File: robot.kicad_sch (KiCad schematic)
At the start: 8 parts, among them IC1 A3901SEJTR-T, J1 MOT1_OUTPUT, J2 MOT2_OUTPUT, J3 CONN_BAT, U1 MOUDLE-SEEEDUINO-XIAO-ESP32C3

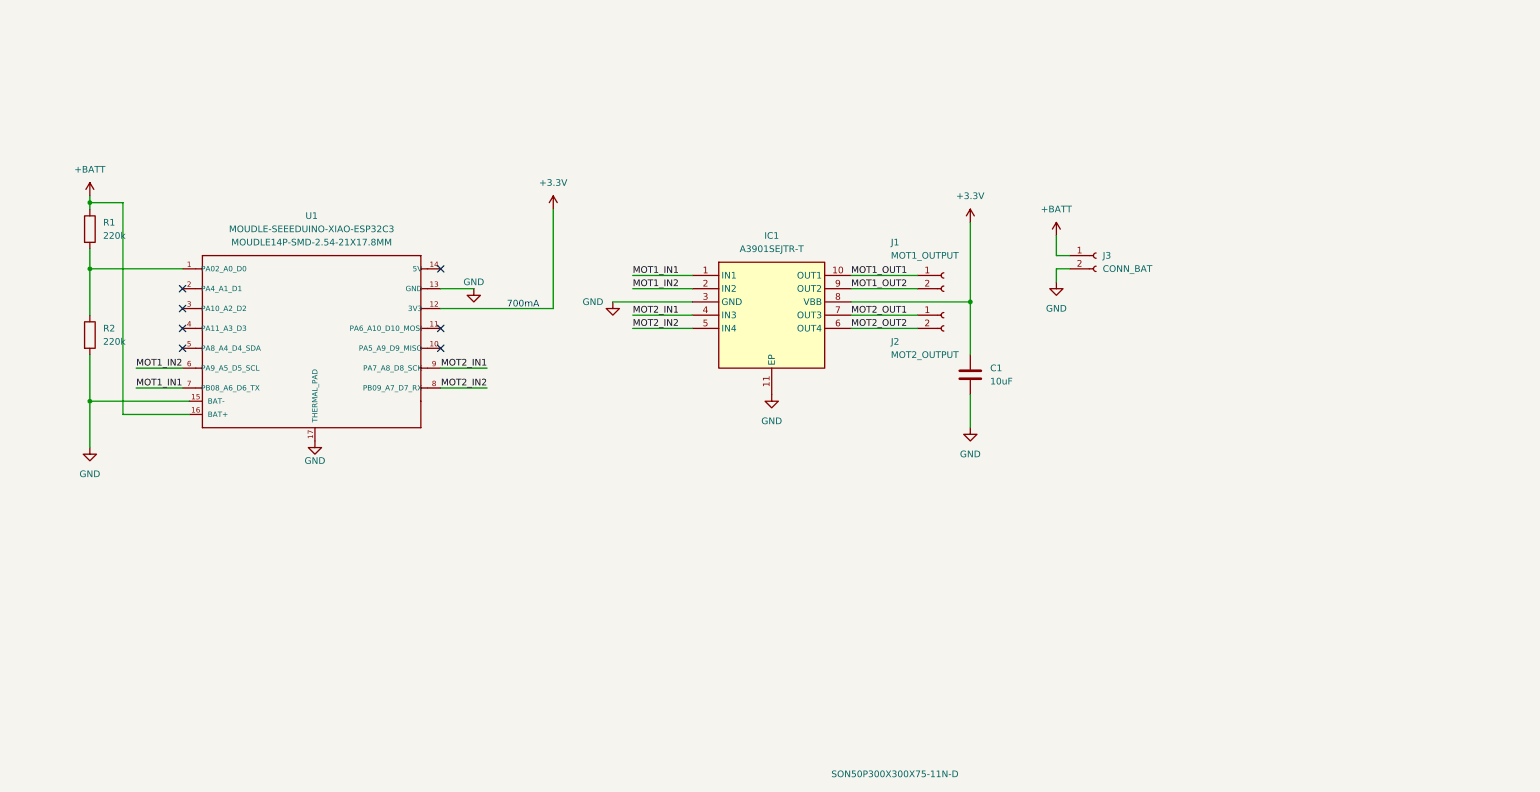
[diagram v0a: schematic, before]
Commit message: add power switch and battery voltage divider
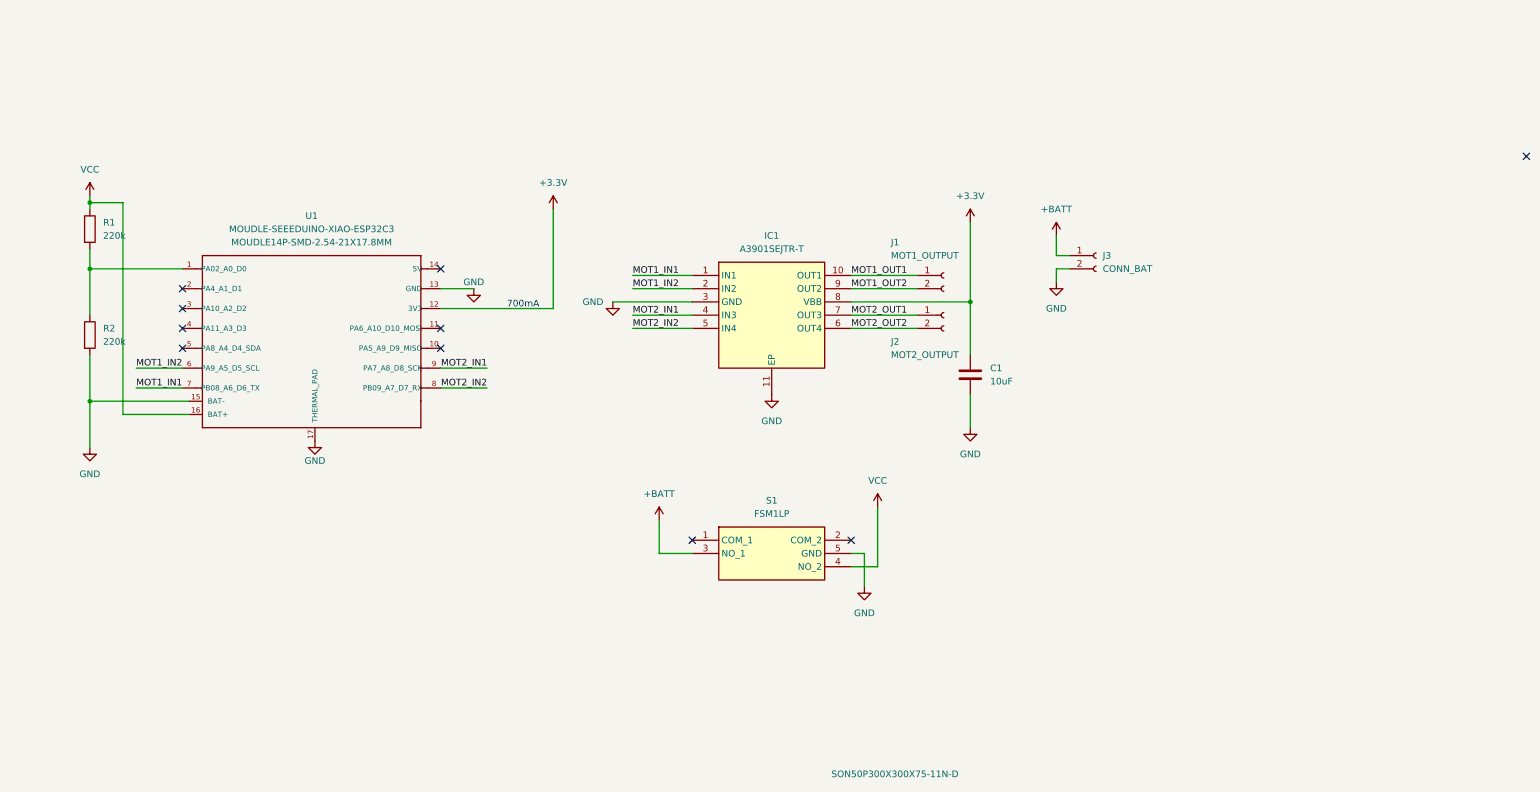
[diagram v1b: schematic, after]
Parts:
- added S1: FSM1LP, FSM1LP, symbol FSM1LP:FSM1LP
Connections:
- net +BATT: now also S1.3 (NO_1); no longer R1.1, U1.16 (BAT+)
- net GND: now also S1.5 (GND)
- new net VCC: R1.1, S1.4 (NO_2), U1.16 (BAT+)
- no-connect marks 7 -> 10
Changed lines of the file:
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@@
   (no_connect (at 74.93 80.01))
   (no_connect (at 74.93 83.82))
+  (no_connect (at 203.2 120.65))
+  (no_connect (at 332.74 46.99))
+  (no_connect (at 172.72 120.65))
   (wire (pts (xy 133.35 91.44) (xy 124.46 91.44))
     (stroke (width 0) (type default))
@@
     (stroke (width 0) (type default))
   )
+  (wire (pts (xy 203.2 125.73) (xy 208.28 125.73))
+    (stroke (width 0) (type default))
+  )
   (wire (pts (xy 203.2 69.85) (xy 215.9 69.85))
     (stroke (width 0) (type default))
@@
     (stroke (width 0) (type default))
   )
+  (wire (pts (xy 166.37 123.19) (xy 172.72 123.19))
+    (stroke (width 0) (type default))
+  )
   (wire (pts (xy 57.15 64.77) (xy 57.15 68.58))
     (stroke (width 0) (type default))
@@
     (stroke (width 0) (type default))
   )
+  (wire (pts (xy 203.2 123.19) (xy 205.74 123.19))
+    (stroke (width 0) (type default))
+  )
   (wire (pts (xy 226.06 92.71) (xy 226.06 99.06))
     (stroke (width 0) (type default))
@@
     (stroke (width 0) (type default))
   )
+  (wire (pts (xy 166.37 116.84) (xy 166.37 123.19))
+    (stroke (width 0) (type default))
+  )
   (wire (pts (xy 226.06 74.93) (xy 226.06 85.09))
     (stroke (width 0) (type default))
@@
     (stroke (width 0) (type default))
   )
+  (wire (pts (xy 208.28 125.73) (xy 208.28 114.3))
+    (stroke (width 0) (type default))
+  )
   (wire (pts (xy 66.04 91.44) (xy 74.93 91.44))
     (stroke (width 0) (type default))
@@
   )
   (wire (pts (xy 146.05 57.15) (xy 146.05 76.2))
+    (stroke (width 0) (type default))
+  )
+  (wire (pts (xy 205.74 123.19) (xy 205.74 129.54))
     (stroke (width 0) (type default))
   )
@@
         (path "/0426a851-9a02-4d3b-8136-e939d046b2a1"
           (reference "#PWR05") (unit 1)
+        )
+      )
+    )
+  )
+  (symbol (lib_id "power:VCC") (at 208.28 114.3 0) (unit 1)
+    (in_bom yes) (on_board yes) (dnp no) (fields_autoplaced)
+    (property "Reference" "#PWR012" (at 208.28 118.11 0)
+      (effects (font (size 1.27 1.27)) hide)
+    )
+    (property "Value" "VCC" (at 208.28 109.22 0)
+      (effects (font (size 1.27 1.27)))
+    )
+    (property "Footprint" "" (at 208.28 114.3 0)
+      (effects (font (size 1.27 1.27)) hide)
+    )
+    (property "Datasheet" "" (at 208.28 114.3 0)
+      (effects (font (size 1.27 1.27)) hide)
+    )
+    (pin "1")
+    (instances
+      (project "robot"
+        (path "/0426a851-9a02-4d3b-8136-e939d046b2a1"
+          (reference "#PWR012") (unit 1)
         )
       )
@@
     )
   )
+  (symbol (lib_id "power:VCC") (at 57.15 54.61 0) (unit 1)
+    (in_bom yes) (on_board yes) (dnp no) (fields_autoplaced)
+    (property "Reference" "#PWR010" (at 57.15 58.42 0)
+      (effects (font (size 1.27 1.27)) hide)
+    )
+    (property "Value" "VCC" (at 57.15 49.53 0)
+      (effects (font (size 1.27 1.27)))
+    )
+    (property "Footprint" "" (at 57.15 54.61 0)
+      (effects (font (size 1.27 1.27)) hide)
+    )
+    (property "Datasheet" "" (at 57.15 54.61 0)
+      (effects (font (size 1.27 1.27)) hide)
+    )
+    (pin "1")
+    (instances
+      (project "robot"
+        (path "/0426a851-9a02-4d3b-8136-e939d046b2a1"
+          (reference "#PWR010") (unit 1)
+        )
+      )
+    )
+  )
   (symbol (lib_id "power:GND") (at 100.33 101.6 0) (unit 1)
     (in_bom yes) (on_board yes) (dnp no)
@@
     )
   )
-  (symbol (lib_id "power:+BATT") (at 57.15 54.61 0) (unit 1)
-    (in_bom yes) (on_board yes) (dnp no) (fields_autoplaced)
-    (property "Reference" "#PWR010" (at 57.15 58.42 0)
-      (effects (font (size 1.27 1.27)) hide)
-    )
-    (property "Value" "+BATT" (at 57.15 49.53 0)
-      (effects (font (size 1.27 1.27)))
-    )
-    (property "Footprint" "" (at 57.15 54.61 0)
-      (effects (font (size 1.27 1.27)) hide)
-    )
-    (property "Datasheet" "" (at 57.15 54.61 0)
-      (effects (font (size 1.27 1.27)) hide)
-    )
-    (pin "1")
-    (instances
-      (project "robot"
-        (path "/0426a851-9a02-4d3b-8136-e939d046b2a1"
-          (reference "#PWR010") (unit 1)
-        )
-      )
-    )
-  )
   (symbol (lib_id "Device:R") (at 57.15 60.96 0) (unit 1)
     (in_bom yes) (on_board yes) (dnp no) (fields_autoplaced)
@@
         )
       )
+    )
+  )
+  (symbol (lib_id "power:+BATT") (at 166.37 116.84 0) (unit 1)
+    (in_bom yes) (on_board yes) (dnp no) (fields_autoplaced)
+    (property "Reference" "#PWR014" (at 166.37 120.65 0)
+      (effects (font (size 1.27 1.27)) hide)
+    )
+    (property "Value" "+BATT" (at 166.37 111.76 0)
+      (effects (font (size 1.27 1.27)))
+    )
+    (property "Footprint" "" (at 166.37 116.84 0)
+      (effects (font (size 1.27 1.27)) hide)
+    )
+    (property "Datasheet" "" (at 166.37 116.84 0)
+      (effects (font (size 1.27 1.27)) hide)
+    )
+    (pin "1")
+    (instances
+      (project "robot"
+        (path "/0426a851-9a02-4d3b-8136-e939d046b2a1"
+          (reference "#PWR014") (unit 1)
+        )
+      )
+    )
+  )
+  (symbol (lib_id "FSM1LP:FSM1LP") (at 172.72 120.65 0) (unit 1)
+    (in_bom yes) (on_board yes) (dnp no) (fields_autoplaced)
+    (property "Reference" "S1" (at 187.96 113.03 0)
+      (effects (font (size 1.27 1.27)))
+    )
+    (property "Value" "FSM1LP" (at 187.96 115.57 0)
+      (effects (font (size 1.27 1.27)))
+    )
+    (property "Footprint" "FSM1LP" (at 199.39 215.57 0)
+      (effects (font (size 1.27 1.27)) (justify left top) hide)
+    )
+    (property "Datasheet" "miluabraham92@gmail.com" (at 199.39 315.57 0)
+      (effects (font (size 1.27 1.27)) (justify left top) hide)
+    )
+    (property "Height" "3.4" (at 199.39 515.57 0)
+      (effects (font (size 1.27 1.27)) (justify left top) hide)
+    )
+    (property "Manufacturer_Name" "TE Connectivity" (at 199.39 615.57 0)
+      (effects (font (size 1.27 1.27)) (justify left top) hide)
+    )
+    (property "Manufacturer_Part_Number" "FSM1LP" (at 199.39 715.57 0)
+      (effects (font (size 1.27 1.27)) (justify left top) hide)
+    )
+    (property "Mouser Part Number" "506-FSM1LP" (at 199.39 815.57 0)
+      (effects (font (size 1.27 1.27)) (justify left top) hide)
+    )
+    (property "Mouser Price/Stock" "https://www.mouser.co.uk/ProductDetail/TE-Connectivity-PB/FSM1LP?qs=X41HXGMJECpfKcLAbtysig%3D%3D" (at 199.39 915.57 0)
+      (effects (font (size 1.27 1.27)) (justify left top) hide)
+    )
+    (property "Arrow Part Number" "FSM1LP" (at 199.39 1015.57 0)
+      (effects (font (size 1.27 1.27)) (justify left top) hide)
+    )
+    (property "Arrow Price/Stock" "https://www.arrow.com/en/products/fsm1lp/te-connectivity?region=nac" (at 199.39 1115.57 0)
+      (effects (font (size 1.27 1.27)) (justify left top) hide)
+    )
+    (pin "2")
+    (pin "1")
+    (pin "5")
+    (pin "4")
+    (pin "3")
+    (instances
+      (project "robot"
+        (path "/0426a851-9a02-4d3b-8136-e939d046b2a1"
+          (reference "S1") (unit 1)
+        )
+      )
+    )
+  )
+  (symbol (lib_id "power:GND") (at 205.74 129.54 0) (unit 1)
+    (in_bom yes) (on_board yes) (dnp no) (fields_autoplaced)
+    (property "Reference" "#PWR013" (at 205.74 135.89 0)
+      (effects (font (size 1.27 1.27)) hide)
+    )
+    (property "Value" "GND" (at 205.74 134.62 0)
+      (effects (font (size 1.27 1.27)))
+    )
+    (property "Footprint" "" (at 205.74 129.54 0)
+      (effects (font (size 1.27 1.27)) hide)
+    )
+    (property "Datasheet" "" (at 205.74 129.54 0)
+      (effects (font (size 1.27 1.27)) hide)
+    )
+    (pin "1")
+    (instances
+      (project "robot"
+        (path "/0426a851-9a02-4d3b-8136-e939d046b2a1"
+          (reference "#PWR013") (unit 1)
+        )
+      )

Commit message: 6-switch dipswitch for misc. configuration
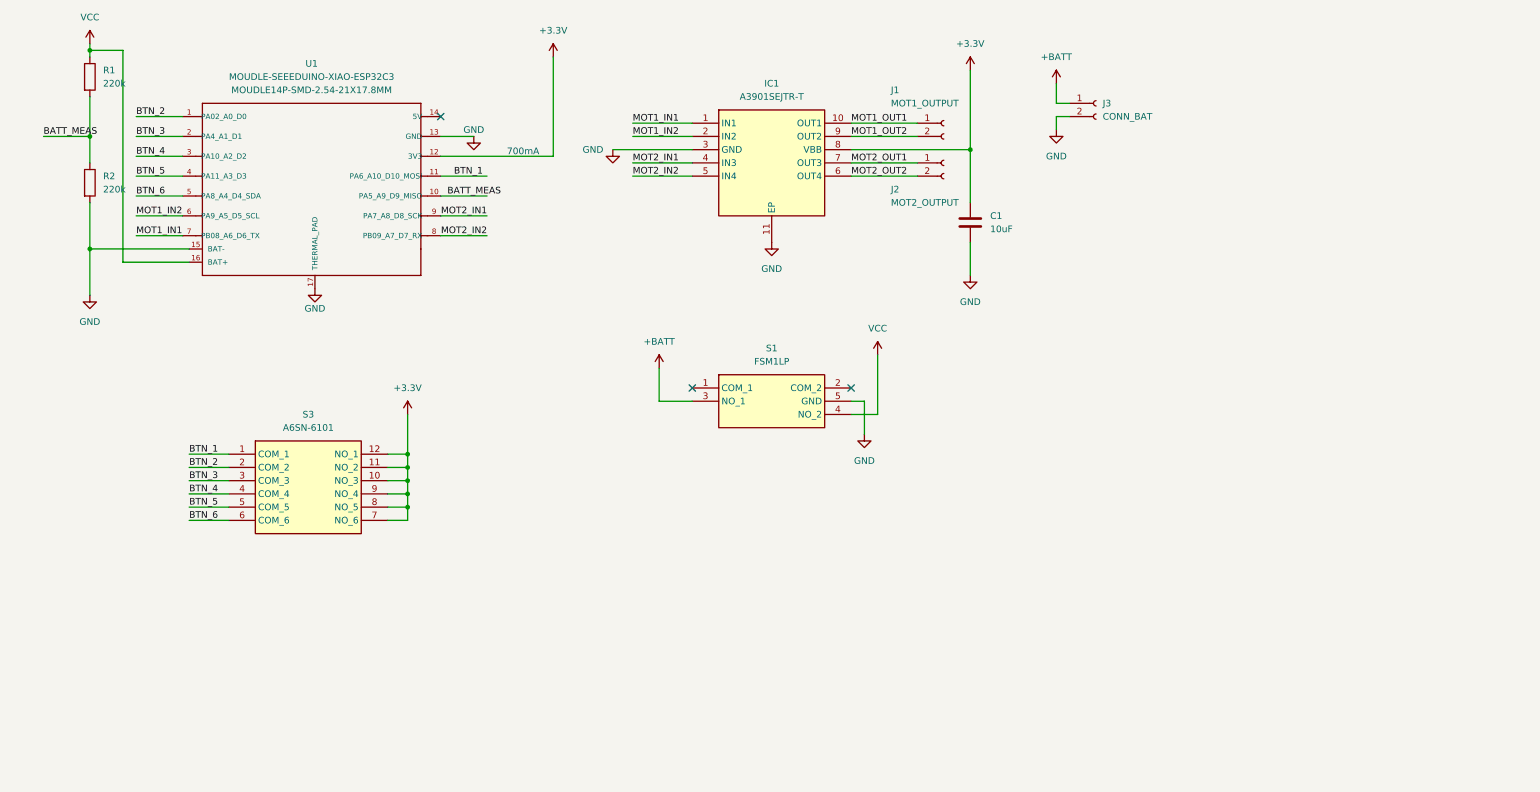
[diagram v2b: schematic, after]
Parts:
- added S3: A6SN-6101, A6SN6101, symbol A6SN-6101:A6SN-6101
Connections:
- net +3.3V: now also S3.10 (NO_3), S3.11 (NO_2), S3.12 (NO_1), S3.7 (NO_6), S3.8 (NO_5), S3.9 (NO_4)
- net BATT_MEAS: now reaches R1.2, R2.1
- net BATT_MEAS: now also U1.10 (PA5_A9_D9_MISO); no longer U1.1 (PA02_A0_D0)
- net BTN_1: now reaches U1.11 (PA6_A10_D10_MOSI)
- net BTN_1: now also S3.1 (COM_1)
- net BTN_3: now reaches U1.2 (PA4_A1_D1)
- net BTN_3: now also S3.3 (COM_3)
- net BTN_4: now reaches U1.3 (PA10_A2_D2)
- net BTN_4: now also S3.4 (COM_4)
- net BTN_5: now reaches U1.4 (PA11_A3_D3)
- net BTN_5: now also S3.5 (COM_5)
- net BTN_6: now reaches U1.5 (PA8_A4_D4_SDA)
- net BTN_6: now also S3.6 (COM_6)
- new net BTN_2: S3.2 (COM_2), U1.1 (PA02_A0_D0)
- no-connect marks 10 -> 3
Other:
- moved on the sheet: C1, IC1, J1, J2, J3, R1, R2, S1, U1

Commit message: 4-switch dipswitch, LEDs, reorder
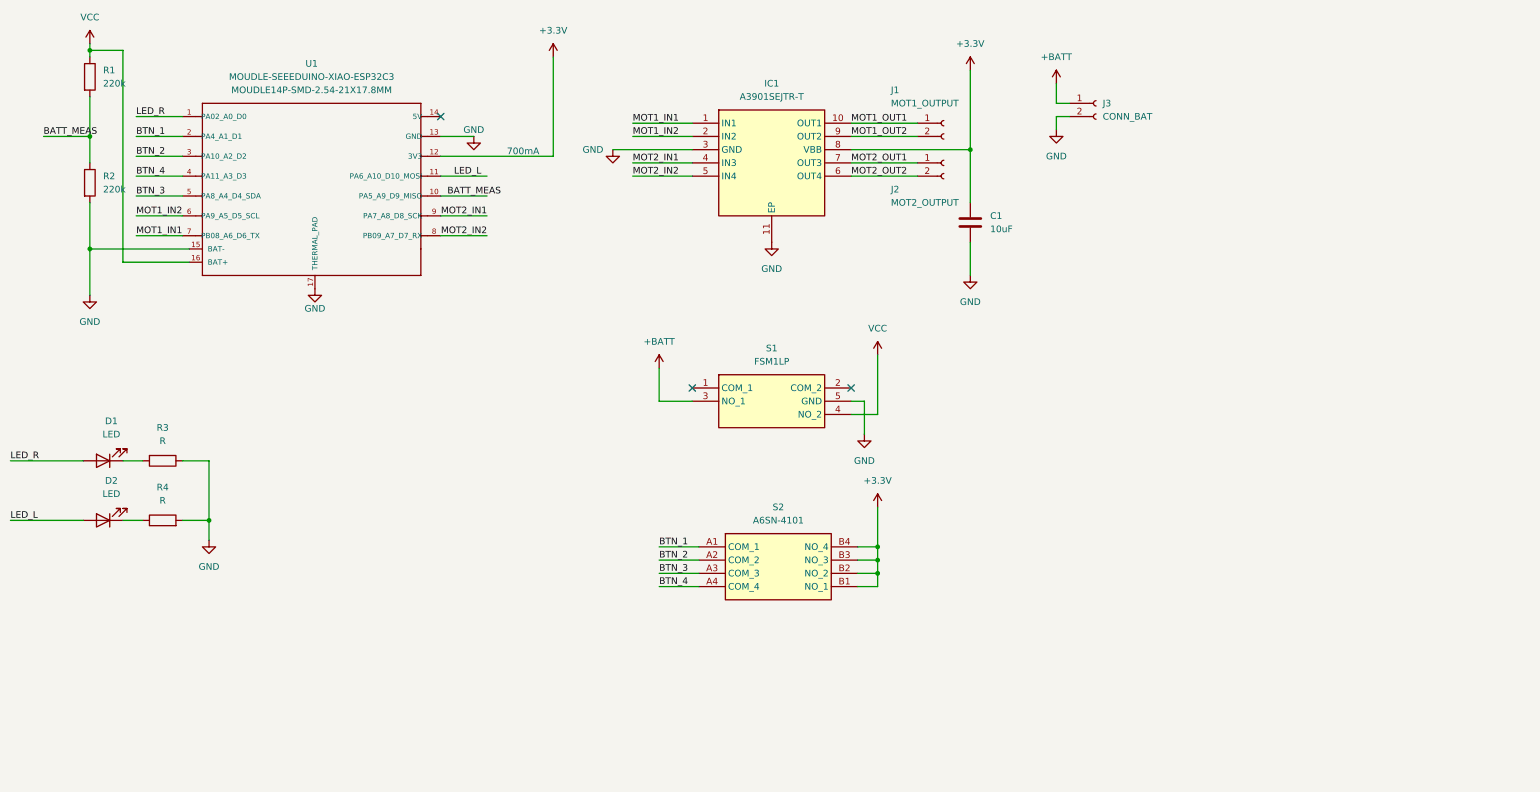
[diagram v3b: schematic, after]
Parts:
- removed S3: A6SN-6101, A6SN6101, symbol A6SN-6101:A6SN-6101
- added D1, D2: LED, LED_SMD:LED_0805_2012Metric_Pad1.15x1.40mm_HandSolder, symbol Device:LED
- added R3, R4: R, Resistor_SMD:R_0603_1608Metric_Pad0.98x0.95mm_HandSolder, symbol Device:R
- added S2: A6SN-4101, A6SN4101, symbol A6SN-4101:A6SN-4101
- C1, R1: footprint Capacitor_SMD:C_0201_0603Metric_Pad0.64x0.40mm_HandSolder -> Capacitor_SMD:C_0603_1608Metric_Pad1.08x0.95mm_HandSolder
- R2: footprint Resistor_SMD:R_0201_0603Metric_Pad0.64x0.40mm_HandSolder -> Resistor_SMD:R_0603_1608Metric_Pad0.98x0.95mm_HandSolder
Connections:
- net BTN_5 is gone; now on net BTN_4: U1.4 (PA11_A3_D3)
- net BTN_6 is gone; now on net BTN_3: U1.5 (PA8_A4_D4_SDA)
- net +3.3V: now also S2.B1 (NO_1), S2.B2 (NO_2), S2.B3 (NO_3), S2.B4 (NO_4)
- net BTN_1: now also U1.2 (PA4_A1_D1), S2.A1 (COM_1); no longer U1.11 (PA6_A10_D10_MOSI)
- net BTN_2: now also U1.3 (PA10_A2_D2), S2.A2 (COM_2); no longer U1.1 (PA02_A0_D0)
- net BTN_3: now also S2.A3 (COM_3); no longer U1.2 (PA4_A1_D1)
- net BTN_4: now also S2.A4 (COM_4); no longer U1.3 (PA10_A2_D2)
- net GND: now also R3.1, R4.2
- new net: D2.1 (K), R4.1
- new net: D1.1 (K), R3.2
- new net LED_L: D2.2 (A), U1.11 (PA6_A10_D10_MOSI)
- new net LED_R: D1.2 (A), U1.1 (PA02_A0_D0)
